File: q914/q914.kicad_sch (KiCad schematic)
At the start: 12 parts, among them J1 5V/2A, J2 To RPi 40pin, SW1 SHUTTER, SW2 SHUTDOWN

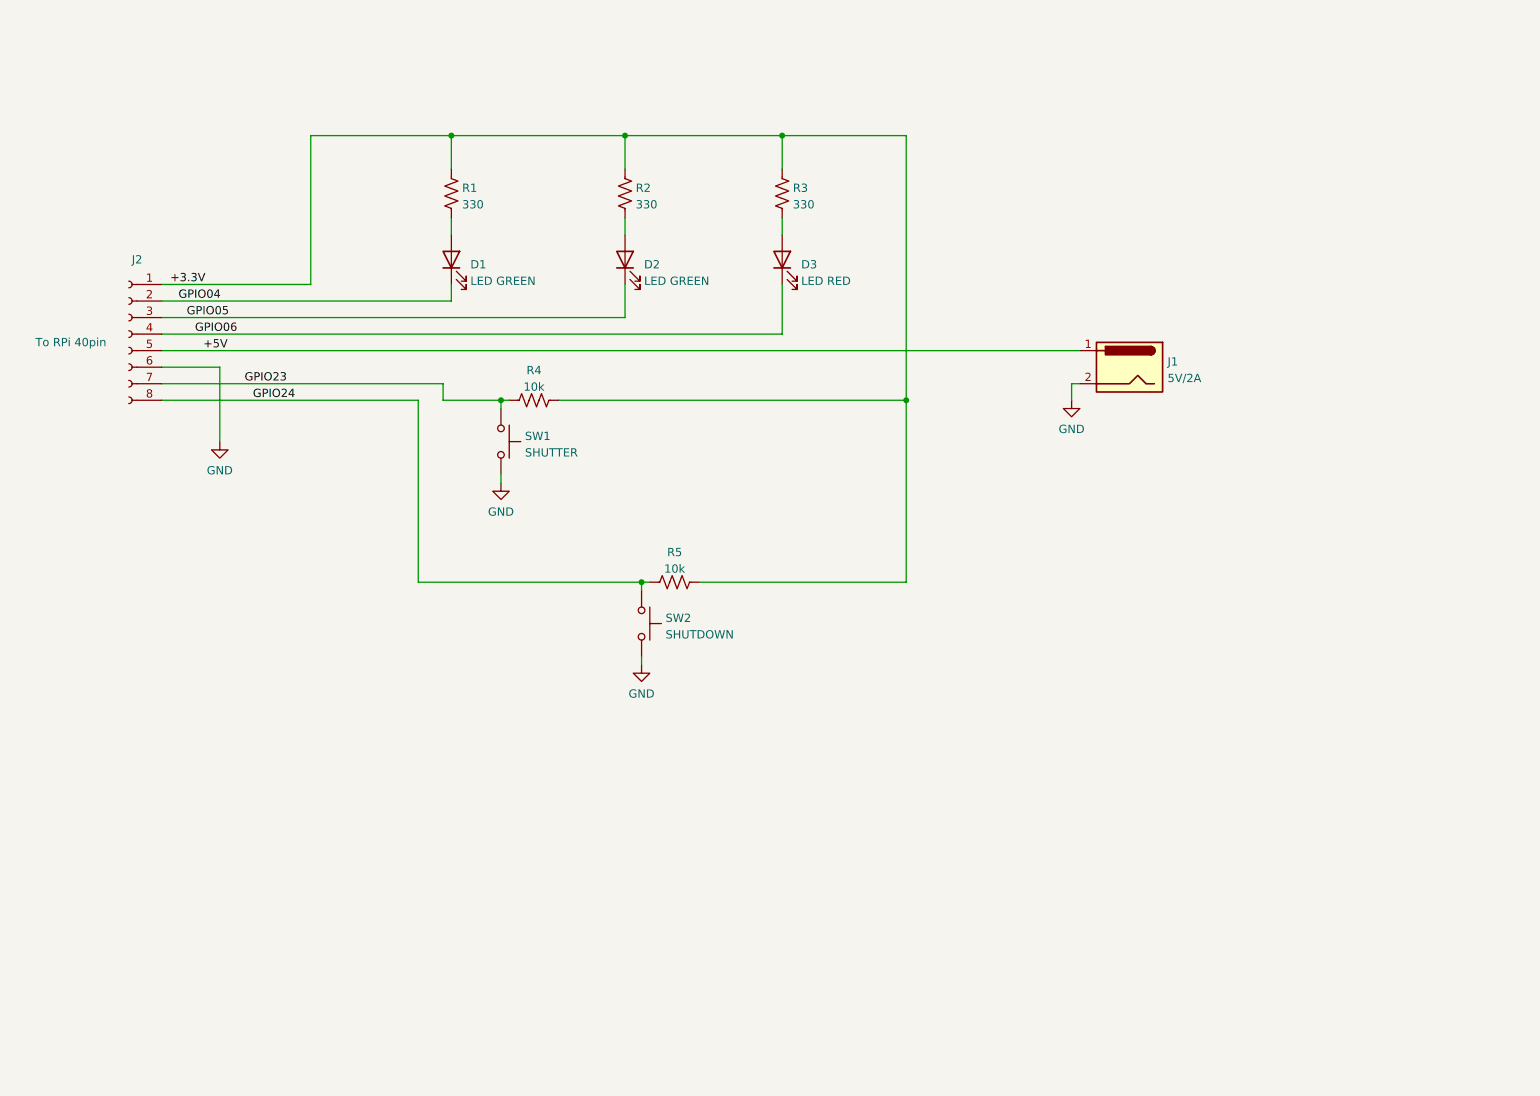
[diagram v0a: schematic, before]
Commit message: Ver2.00 超音波距離測定回路
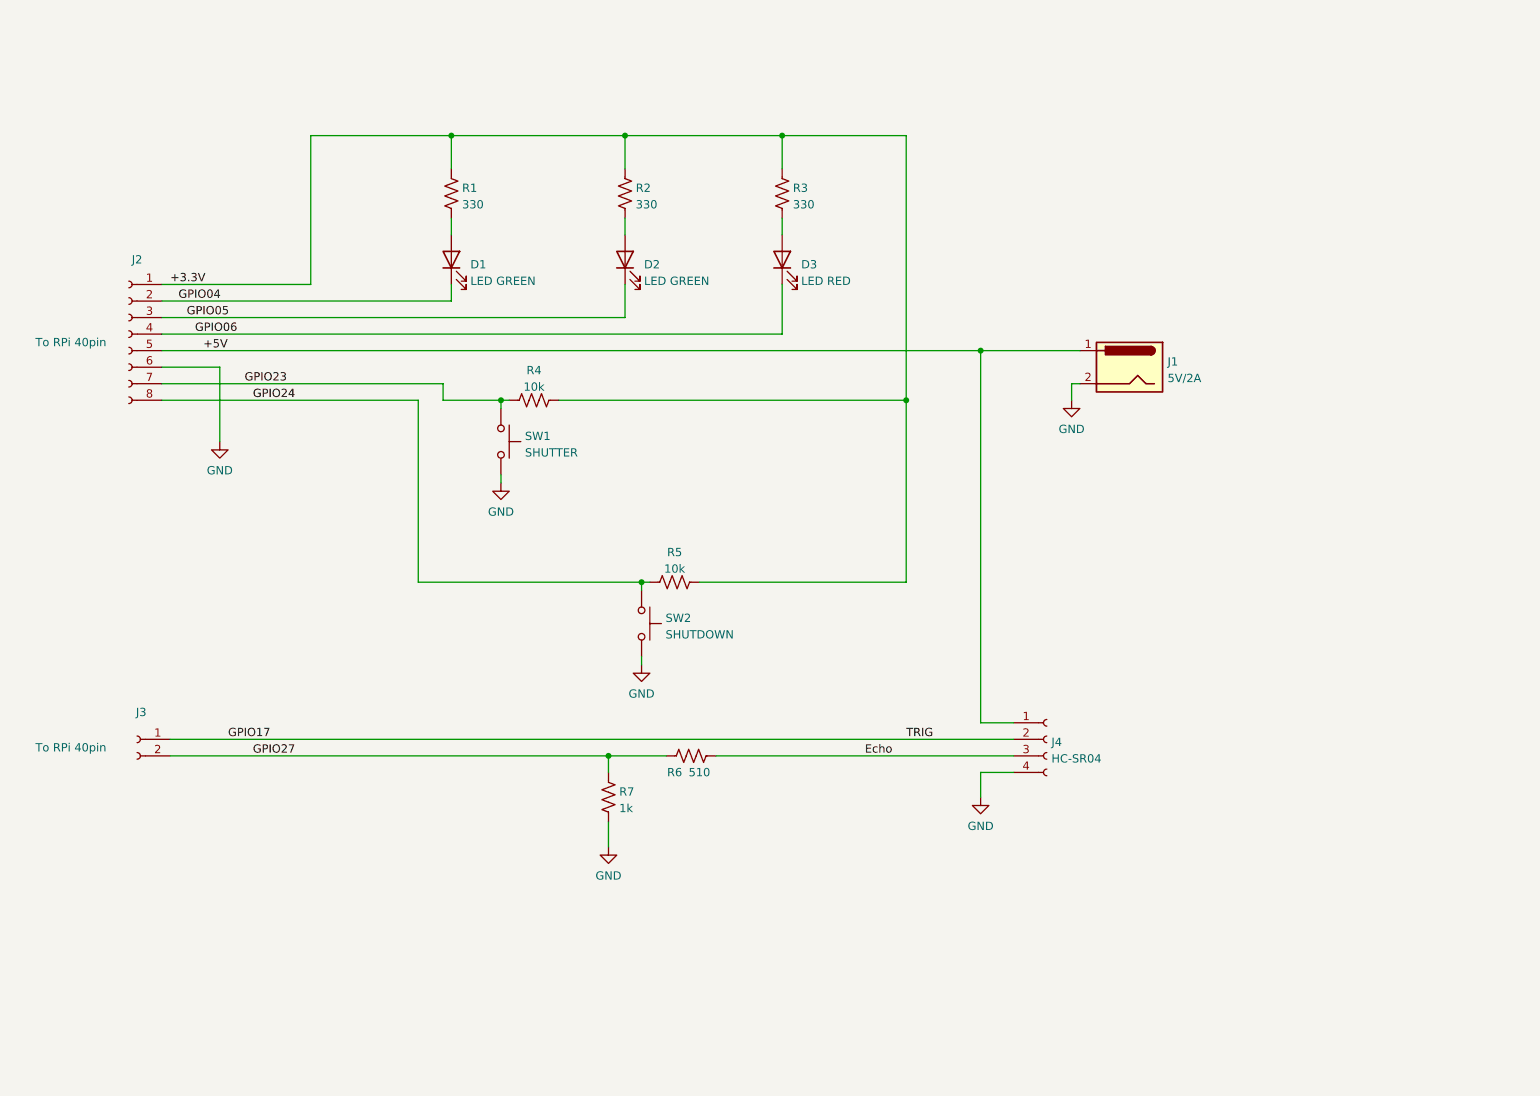
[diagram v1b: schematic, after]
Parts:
- added J3: To RPi 40pin, symbol Connector:Conn_01x02_Female
- added J4: HC-SR04, symbol Connector:Conn_01x04_Female
- added R6: 510, symbol Device:R_US
- added R7: 1k, symbol Device:R_US
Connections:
- net +5V: now also J4.1 (Pin_1)
- net GND: now also J4.4 (Pin_4), R7.2
- new net Echo: J4.3 (Pin_3), R6.2
- new net GPIO17: J3.1 (Pin_1), J4.2 (Pin_2)
- new net GPIO27: J3.2 (Pin_2), R6.1, R7.1
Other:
- company: AMPSD Kyushu Univ. -> AMPSD Kyushu Univ. Designed by M.Horimoto
- title: CuCuCam Interface circuit -> QCamVer
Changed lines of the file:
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@@
   (paper "A4")
   (title_block
-    (title "CuCuCam Interface circuit")
-    (date "2022-04-17")
-    (rev "1.00")
-    (company "AMPSD Kyushu Univ.")
-    (comment 1 "but will be mounted by hand on a Universal board.")
-    (comment 2 "This circuit is not planned to be made into a PCB, ")
+    (title "QCamVer")
+    (date "2022-04-25")
+    (rev "2.00")
+    (company "AMPSD Kyushu Univ. Designed by M.Horimoto")
   )
   (junction (at 129.54 50.8) (diameter 0) (color 0 0 0 0)
   )
+  (junction (at 184.15 83.82) (diameter 0) (color 0 0 0 0)
+  )
   (junction (at 172.72 91.44) (diameter 0) (color 0 0 0 0)
   )
@@
   (junction (at 132.08 119.38) (diameter 0) (color 0 0 0 0)
   )
+  (junction (at 127 146.05) (diameter 0) (color 0 0 0 0)
+  )
   (junction (at 110.49 91.44) (diameter 0) (color 0 0 0 0)
   )
@@
     (stroke (width 0) (type default) (color 0 0 0 0))
   )
+  (wire (pts (xy 184.15 83.82) (xy 199.39 83.82))
+    (stroke (width 0) (type default) (color 0 0 0 0))
+  )
   (wire (pts (xy 58.42 76.2) (xy 102.87 76.2))
     (stroke (width 0) (type default) (color 0 0 0 0))
   )
+  (wire (pts (xy 59.69 143.51) (xy 189.23 143.51))
+    (stroke (width 0) (type default) (color 0 0 0 0))
+  )
   (wire (pts (xy 81.28 73.66) (xy 58.42 73.66))
     (stroke (width 0) (type default) (color 0 0 0 0))
@@
     (stroke (width 0) (type default) (color 0 0 0 0))
   )
+  (wire (pts (xy 184.15 140.97) (xy 184.15 83.82))
+    (stroke (width 0) (type default) (color 0 0 0 0))
+  )
   (wire (pts (xy 111.76 91.44) (xy 110.49 91.44))
     (stroke (width 0) (type default) (color 0 0 0 0))
@@
     (stroke (width 0) (type default) (color 0 0 0 0))
   )
+  (wire (pts (xy 127 146.05) (xy 135.89 146.05))
+    (stroke (width 0) (type default) (color 0 0 0 0))
+  )
   (wire (pts (xy 198.12 88.9) (xy 198.12 91.44))
     (stroke (width 0) (type default) (color 0 0 0 0))
@@
     (stroke (width 0) (type default) (color 0 0 0 0))
   )
-  (wire (pts (xy 58.42 83.82) (xy 199.39 83.82))
+  (wire (pts (xy 58.42 83.82) (xy 184.15 83.82))
     (stroke (width 0) (type default) (color 0 0 0 0))
   )
@@
     (stroke (width 0) (type default) (color 0 0 0 0))
   )
+  (wire (pts (xy 127 156.21) (xy 127 160.02))
+    (stroke (width 0) (type default) (color 0 0 0 0))
+  )
   (wire (pts (xy 101.6 88.9) (xy 58.42 88.9))
     (stroke (width 0) (type default) (color 0 0 0 0))
   )
+  (wire (pts (xy 127 146.05) (xy 127 148.59))
+    (stroke (width 0) (type default) (color 0 0 0 0))
+  )
   (wire (pts (xy 133.35 119.38) (xy 132.08 119.38))
     (stroke (width 0) (type default) (color 0 0 0 0))
   )
+  (wire (pts (xy 59.69 146.05) (xy 127 146.05))
+    (stroke (width 0) (type default) (color 0 0 0 0))
+  )
+  (wire (pts (xy 184.15 148.59) (xy 184.15 152.4))
+    (stroke (width 0) (type default) (color 0 0 0 0))
+  )
+  (wire (pts (xy 143.51 146.05) (xy 189.23 146.05))
+    (stroke (width 0) (type default) (color 0 0 0 0))
+  )
   (wire (pts (xy 102.87 73.66) (xy 102.87 76.2))
     (stroke (width 0) (type default) (color 0 0 0 0))
@@
     (stroke (width 0) (type default) (color 0 0 0 0))
   )
+  (wire (pts (xy 189.23 140.97) (xy 184.15 140.97))
+    (stroke (width 0) (type default) (color 0 0 0 0))
+  )
   (wire (pts (xy 153.67 50.8) (xy 153.67 55.88))
     (stroke (width 0) (type default) (color 0 0 0 0))
@@
     (stroke (width 0) (type default) (color 0 0 0 0))
   )
+  (wire (pts (xy 189.23 148.59) (xy 184.15 148.59))
+    (stroke (width 0) (type default) (color 0 0 0 0))
+  )
   (wire (pts (xy 101.6 91.44) (xy 101.6 88.9))
     (stroke (width 0) (type default) (color 0 0 0 0))
@@
     (effects (font (size 1.27 1.27)) (justify left bottom))
   )
+  (label "TRIG" (at 172.72 143.51 0)
+    (effects (font (size 1.27 1.27)) (justify left bottom))
+  )
+  (label "Echo" (at 166.37 146.05 0)
+    (effects (font (size 1.27 1.27)) (justify left bottom))
+  )
+  (label "GPIO17" (at 68.58 143.51 0)
+    (effects (font (size 1.27 1.27)) (justify left bottom))
+  )
   (label "GPIO24" (at 72.39 91.44 0)
+    (effects (font (size 1.27 1.27)) (justify left bottom))
+  )
+  (label "GPIO27" (at 72.39 146.05 0)
     (effects (font (size 1.27 1.27)) (justify left bottom))
   )
@@
     )
     (pin "1")
+  )
+  (symbol (lib_id "Connector:Conn_01x02_Female") (at 54.61 143.51 0) (mirror y) (unit 1)
+    (in_bom yes) (on_board yes)
+    (property "Reference" "J3" (id 0) (at 55.245 139.353 0))
+    (property "Value" "To RPi 40pin" (id 1) (at 44.45 144.78 0))
+    (property "Footprint" "" (id 2) (at 54.61 143.51 0)
+      (effects (font (size 1.27 1.27)) hide)
+    )
+    (property "Datasheet" "~" (id 3) (at 54.61 143.51 0)
+      (effects (font (size 1.27 1.27)) hide)
+    )
+    (pin "1")
+    (pin "2")
   )
   (symbol (lib_id "Device:R_US") (at 115.57 91.44 90) (unit 1)
@@
     )
     (property "Datasheet" "~" (id 3) (at 153.67 59.69 0)
+      (effects (font (size 1.27 1.27)) hide)
+    )
+    (pin "1")
+    (pin "2")
+  )
+  (symbol (lib_id "Device:R_US") (at 139.7 146.05 90) (unit 1)
+    (in_bom yes) (on_board yes)
+    (property "Reference" "R6" (id 0) (at 137.16 148.59 90))
+    (property "Value" "510" (id 1) (at 140.97 148.59 90))
+    (property "Footprint" "" (id 2) (at 139.954 145.034 90)
+      (effects (font (size 1.27 1.27)) hide)
+    )
+    (property "Datasheet" "~" (id 3) (at 139.7 146.05 0)
       (effects (font (size 1.27 1.27)) hide)
     )
@@
     (pin "2")
   )
+  (symbol (lib_id "power:GND") (at 184.15 152.4 0) (unit 1)
+    (in_bom yes) (on_board yes) (fields_autoplaced)
+    (property "Reference" "#PWR?" (id 0) (at 184.15 158.75 0)
+      (effects (font (size 1.27 1.27)) hide)
+    )
+    (property "Value" "GND" (id 1) (at 184.15 156.8434 0))
+    (property "Footprint" "" (id 2) (at 184.15 152.4 0)
+      (effects (font (size 1.27 1.27)) hide)
+    )
+    (property "Datasheet" "" (id 3) (at 184.15 152.4 0)
+      (effects (font (size 1.27 1.27)) hide)
+    )
+    (pin "1")
+  )
   (symbol (lib_id "power:GND") (at 198.12 91.44 0) (unit 1)
     (in_bom yes) (on_board yes) (fields_autoplaced)
@@
     (pin "2")
   )
+  (symbol (lib_id "Device:R_US") (at 127 152.4 0) (unit 1)
+    (in_bom yes) (on_board yes) (fields_autoplaced)
+    (property "Reference" "R7" (id 0) (at 128.651 151.5653 0)
+      (effects (font (size 1.27 1.27)) (justify left))
+    )
+    (property "Value" "1k" (id 1) (at 128.651 154.1022 0)
+      (effects (font (size 1.27 1.27)) (justify left))
+    )
+    (property "Footprint" "" (id 2) (at 128.016 152.654 90)
+      (effects (font (size 1.27 1.27)) hide)
+    )
+    (property "Datasheet" "~" (id 3) (at 127 152.4 0)
+      (effects (font (size 1.27 1.27)) hide)
+    )
+    (pin "1")
+    (pin "2")
+  )
   (symbol (lib_id "Device:R_US") (at 102.87 59.69 0) (unit 1)
     (in_bom yes) (on_board yes) (fields_autoplaced)
@@
     (pin "1")
     (pin "2")
+  )
+  (symbol (lib_id "power:GND") (at 127 160.02 0) (unit 1)
+    (in_bom yes) (on_board yes) (fields_autoplaced)
+    (property "Reference" "#PWR?" (id 0) (at 127 166.37 0)
+      (effects (font (size 1.27 1.27)) hide)
+    )
+    (property "Value" "GND" (id 1) (at 127 164.4634 0))
+    (property "Footprint" "" (id 2) (at 127 160.02 0)
+      (effects (font (size 1.27 1.27)) hide)
+    )
+    (property "Datasheet" "" (id 3) (at 127 160.02 0)
+      (effects (font (size 1.27 1.27)) hide)
+    )
+    (pin "1")
   )
   (symbol (lib_id "Device:R_US") (at 137.16 119.38 90) (unit 1)
@@
     (pin "2")
   )
+  (symbol (lib_id "Connector:Conn_01x04_Female") (at 194.31 143.51 0) (unit 1)
+    (in_bom yes) (on_board yes) (fields_autoplaced)
+    (property "Reference" "J4" (id 0) (at 195.0212 143.9453 0)
+      (effects (font (size 1.27 1.27)) (justify left))
+    )
+    (property "Value" "HC-SR04" (id 1) (at 195.0212 146.4822 0)
+      (effects (font (size 1.27 1.27)) (justify left))
+    )
+    (property "Footprint" "" (id 2) (at 194.31 143.51 0)
+      (effects (font (size 1.27 1.27)) hide)
+    )
+    (property "Datasheet" "~" (id 3) (at 194.31 143.51 0)
+      (effects (font (size 1.27 1.27)) hide)
+    )
+    (pin "1")
+    (pin "2")
+    (pin "3")
+    (pin "4")
+  )
   (symbol (lib_id "power:GND") (at 67.31 97.79 0) (unit 1)
     (in_bom yes) (on_board yes) (fields_autoplaced)
@@
       (reference "#PWR?") (unit 1) (value "GND") (footprint "")
     )
+    (path "/753633ed-c365-425b-81b3-bd233befd3b8"
+      (reference "#PWR?") (unit 1) (value "GND") (footprint "")
+    )
     (path "/7a80751e-a6bc-4ba0-acb2-880e06fac320"
       (reference "#PWR?") (unit 1) (value "GND") (footprint "")
     )
+    (path "/db7a8589-c98b-47bf-9c5e-44710aac0962"
+      (reference "#PWR?") (unit 1) (value "GND") (footprint "")
+    )
     (path "/fa539b66-47b0-4ac1-8912-3d9af7187779"
       (reference "#PWR?") (unit 1) (value "GND") (footprint "")
@@
       (reference "J2") (unit 1) (value "To RPi 40pin") (footprint "")
     )
+    (path "/19bbdaf3-224a-4f8e-a5bb-f7a92d14e018"
+      (reference "J3") (unit 1) (value "To RPi 40pin") (footprint "")
+    )
+    (path "/e70948cf-44fe-4777-a44b-96651998f90f"
+      (reference "J4") (unit 1) (value "HC-SR04") (footprint "")
+    )
     (path "/a4aa2fbd-3cb2-4179-80b8-75d7a8b8dd7f"
       (reference "R1") (unit 1) (value "330") (footprint "")
@@
       (reference "R5") (unit 1) (value "10k") (footprint "")
     )
+    (path "/42f73789-ccca-4e18-844b-499235d89cac"
+      (reference "R6") (unit 1) (value "510") (footprint "")
+    )
+    (path "/93c69ef9-1770-4581-b1e1-5081ba33f1fa"
+      (reference "R7") (unit 1) (value "1k") (footprint "")
+    )
     (path "/c2bebfe4-a61c-45b1-b96a-44047619dd45"

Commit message: Ver 4.00
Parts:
- added J5 (x2): ~, symbol Connector:Conn_01x02_Female
- added J6: ~, symbol Connector:Conn_01x04_Female
- added R8: 510, symbol Device:R_US
- added R9: 1k, symbol Device:R_US
- added RV1, RV2: B10k, symbol Device:R_Potentiometer_US
- added U1: ADS1115, symbol Adafruit:ADS1115
- J3: value To RPi 40pin -> ~
- J4: value HC-SR04 -> ~
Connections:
- net +3.3V: now also RV1.3, RV2.3, U1.1 (Vdd)
- net +5V: now also J6.1 (Pin_1)
- net Echo: now also J6.3 (Pin_3), R8.2
- net GND: now also J6.4 (Pin_4), R9.2, RV1.1, RV2.1, U1.2 (GND)
- net GPIO17 renamed GPIO12
- net GPIO12: now also J5.1 (Pin_1), J6.2 (Pin_2)
- new net: RV2.2, U1.8 (A1)
- new net: RV1.2, U1.7 (A0)
- new net GPIO16: J5.2 (Pin_2), R8.1, R9.1
- new net SCL: J5.1 (Pin_1), U1.3 (SCL)
- new net SDA: J5.2 (Pin_2), U1.4 (SDA)
- no-connect marks 0 -> 4
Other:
- note added: "To SR04 for Distance target"
- note added: "To SR04 for Height"
- note added: "仰角(Elevation angle)"
- note added: "方位角(Azimuth)"
